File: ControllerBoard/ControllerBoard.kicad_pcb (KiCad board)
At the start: 4 copper layers, 34 x 12 mm, 31 parts, among them J1 X0511WVS-24AS-LPV01, J2 X0511WVS-24AS-LPV01, U1 PLP5860RKPR, U2 LIS2DE12, U3 nRF52810-QCxx, Y1 32.768kHz 12.5pF, Y2 32MHz 8pF <40ppm

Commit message: Minor board updates
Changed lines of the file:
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@@
   (segment (start 135.27 76.75) (end 135.309081 76.789081) (width 0.2) (layer "B.Cu") (net 6))
   (arc (start 135.309081 76.789081) (mid 135.450381 77.000552) (end 135.5 77.25) (width 0.2) (layer "B.Cu") (net 6))
+  (segment (start 134 85.25) (end 134 85.75) (width 0.2) (layer "F.Cu") (net 7))
+  (segment (start 135 82.95) (end 135 84.25) (width 0.2) (layer "F.Cu") (net 7))
   (segment (start 134 86.23) (end 134 85.75) (width 0.2) (layer "F.Cu") (net 7))
   (segment (start 132.75 86.23) (end 134 86.23) (width 0.2) (layer "F.Cu") (net 7))
   (segment (start 135 84.25) (end 134 85.25) (width 0.2) (layer "F.Cu") (net 7))
-  (segment (start 135 82.95) (end 135 84.25) (width 0.2) (layer "F.Cu") (net 7))
-  (segment (start 134 85.25) (end 134 85.75) (width 0.2) (layer "F.Cu") (net 7))
   (segment (start 136.5 86.23) (end 136.5 85.75) (width 0.2) (layer "F.Cu") (net 8))
-  (segment (start 135.5 84.375) (end 136.5 85.375) (width 0.2) (layer "F.Cu") (net 8))
-  (segment (start 135.5 82.95) (end 135.5 84.375) (width 0.2) (layer "F.Cu") (net 8))
+  (segment (start 135.5 82.95) (end 135.5 84.25) (width 0.2) (layer "F.Cu") (net 8))
+  (segment (start 135.5 84.25) (end 136.5 85.25) (width 0.2) (layer "F.Cu") (net 8))
+  (segment (start 136.5 85.25) (end 136.5 85.75) (width 0.2) (layer "F.Cu") (net 8))
   (segment (start 137.75 86.23) (end 136.5 86.23) (width 0.2) (layer "F.Cu") (net 8))
-  (segment (start 136.5 85.375) (end 136.5 85.75) (width 0.2) (layer "F.Cu") (net 8))
   (segment (start 134.5 83.58) (end 133.98 84.1) (width 0.2) (layer "F.Cu") (net 9))
   (segment (start 134.5 82.95) (end 134.5 83.58) (width 0.2) (layer "F.Cu") (net 9))

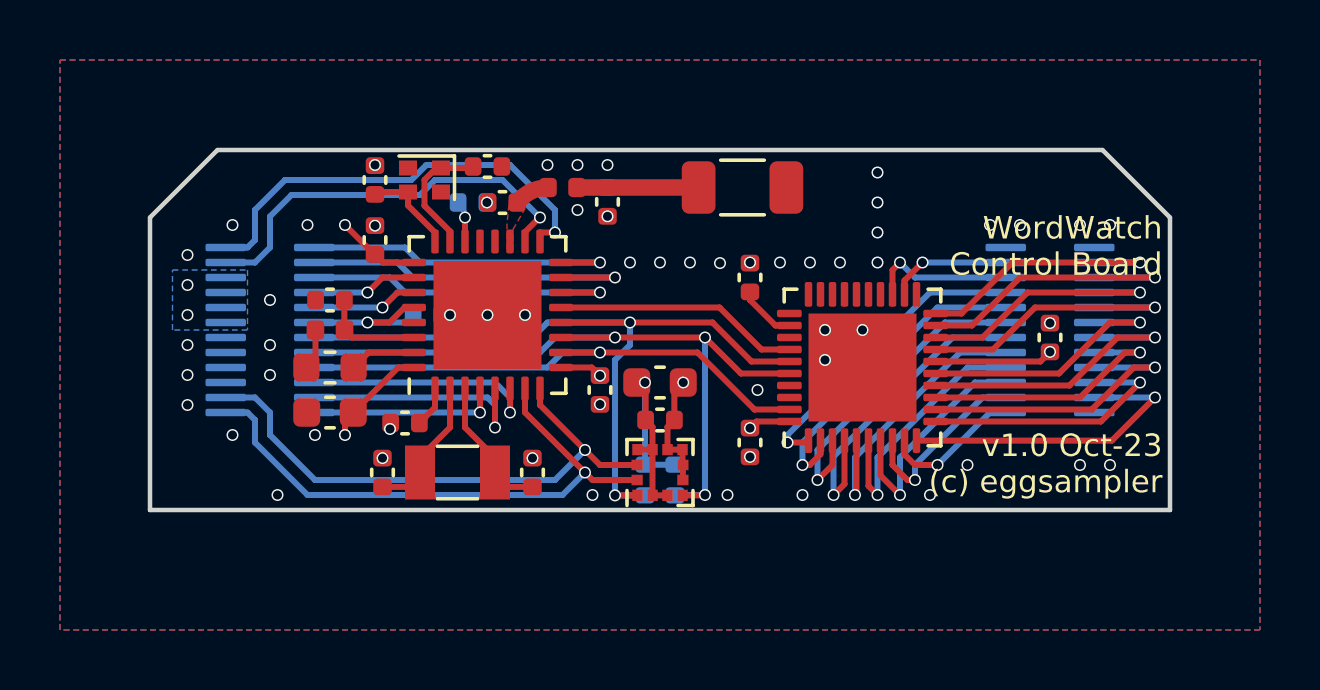
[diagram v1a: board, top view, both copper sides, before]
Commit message: Remove LED driver
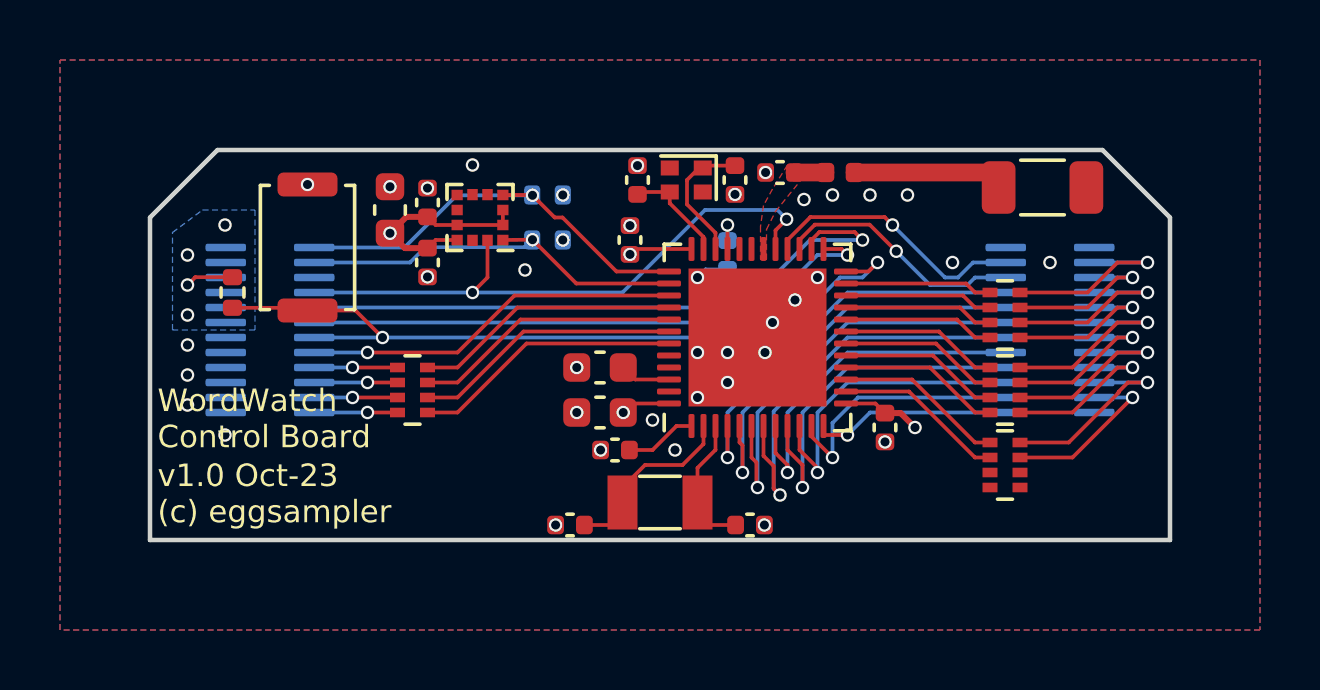
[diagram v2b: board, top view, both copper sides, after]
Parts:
- removed C17: 16p, Capacitor_SMD:C_0402_1005Metric
- removed C18: 10n, Capacitor_SMD:C_0402_1005Metric
- removed C2, C3: 1u, Capacitor_SMD:C_0402_1005Metric
- removed L2: 10uH, Inductor_SMD:L_0603_1608Metric
- removed L3: 3.9nH, Inductor_SMD:L_0402_1005Metric
- removed U1: PLP5860RKPR, Package_DFN_QFN:QFN-40-1EP_5x5mm_P0.4mm_EP3.6x3.6mm
- added R3: 4.7k, Resistor_SMD:R_0402_1005Metric, F.Cu at (127.8, 79.8)
- added RN1: 1k, Resistor_SMD:R_Array_Concave_4x0402, F.Cu at (153.5, 85.5)
- added RN2: 1k, Resistor_SMD:R_Array_Concave_4x0402, F.Cu at (153.5, 83.0)
- added RN3: 1k, Resistor_SMD:R_Array_Concave_4x0402, F.Cu at (153.5, 80.5)
- added RN4: 1k, Resistor_SMD:R_Array_Concave_4x0402, F.Cu at (133.8, 83.0)
- added SW1: RESET, Button_Switch_SMD:SW_Push_SPST_NO_Alps_SKRK, F.Cu at (130.2, 78.2)
- C1: value 1u -> 100n
- C11: value 100n -> 100p; moved to B.Cu
- C12: value 25p -> 12p
- C15: value 0.8p -> 12p
- C16: value 16p -> 12p
- C6: footprint Capacitor_SMD:C_0402_1005Metric -> Capacitor_SMD:C_0603_1608Metric
- C7: value 100p -> 12p; moved to F.Cu
- C8: value 25p -> 4.7u; footprint Capacitor_SMD:C_0402_1005Metric -> Capacitor_SMD:C_0603_1608Metric
- C9: value 4.7u -> 100n; footprint Capacitor_SMD:C_0603_1608Metric -> Capacitor_SMD:C_0402_1005Metric
- L1: value 15nH -> 3.9nH
- U3: value nRF52810-QCxx -> nRF52810-QFxx; footprint Package_DFN_QFN:QFN-32-1EP_5x5mm_P0.5mm_EP3.6x3.6mm -> Package_DFN_QFN:QFN-48-1EP_6x6mm_P0.4mm_EP4.6x4.6mm
- Y1: value 32.768kHz 12.5pF -> 32.768kHz
- Y2: value 32MHz 8pF <40ppm -> 32MHz
- moved C1 20.9 mm to (134.2, 78.8), turned to -90 degrees
- moved C10 18.1 mm to (149.5, 84.2), turned to -90 degrees
- moved L1 17.8 mm to (148.0, 75.8)
- moved C9 11.5 mm to (141.0, 78.0), turned to 90 degrees
- moved C7 11.2 mm to (139.0, 87.5), turned to 180 degrees
- moved C5 10.7 mm to (133.0, 77.0), turned to 90 degrees
- moved C4 10.6 mm to (134.2, 76.8), turned to 90 degrees
- moved R1 10.4 mm to (138.2, 76.5), turned to 0 degrees
- moved U2 10.4 mm to (136.0, 77.2), turned to 180 degrees
- moved AE1 10.0 mm to (154.8, 76.2)
- moved C6 9.28 mm to (140.0, 82.2)
- moved U3 9.03 mm to (145.2, 81.2)
- moved Y2 8.72 mm to (142.9, 76.0)
- moved R2 8.63 mm to (138.2, 78.0), turned to 180 degrees
- moved C15 7.79 mm to (144.5, 76.0), turned to 90 degrees
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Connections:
- C11 pad 1: VCC -> /Microcontroller/DEC3
- C12 pad 1: GND -> /Microcontroller/XL2
- C12 pad 2: /Microcontroller/XL2 -> GND
- C14 pad 1: /Microcontroller/ANT2 -> /Microcontroller/ANT1
- C15 pad 1: /Microcontroller/ANT1 -> GND
- C15 pad 2: GND -> /Microcontroller/XC1
- C16 pad 2: /Microcontroller/XC1 -> /Microcontroller/XC2
- C7 pad 1: /Microcontroller/DEC3 -> /Microcontroller/XL1
- C8 pad 1: GND -> VCC
- C8 pad 2: /Microcontroller/XL1 -> GND
- J2 pad 1: /Connectors/RESET -> /Accelerometer/SDA
- J2 pad 11: /Connectors/VSENSE -> /Connectors/SWDCLK
- J2 pad 13: /Accelerometer/SCL -> /Microcontroller/RESET
- J2 pad 15: /Accelerometer/SDA -> /Connectors/BUTTON
- J2 pad 17: /Connectors/LED_EN -> /Connectors/LED0
- J2 pad 19: /Connectors/LED2 -> /Connectors/LED1
- J2 pad 2: /Connectors/SWDCLK -> VCC
- J2 pad 21: /Connectors/LED3 -> /Connectors/LED2
- J2 pad 22: /Accelerometer/INT2 -> GND
- J2 pad 23: /Connectors/BUTTON -> /Connectors/LED3
- J2 pad 24: /Accelerometer/INT1 -> GND
- J2 pad 3: /Connectors/TX -> /Accelerometer/SCL
- J2 pad 4: /Connectors/SWDIO -> VCC
- J2 pad 5: /Connectors/RX -> GND
- J2 pad 7: /Connectors/LED0 -> /Accelerometer/INT1
- J2 pad 9: /Connectors/LED1 -> /Connectors/SWDIO
- L1 pad 1: /Microcontroller/DEC4 -> /Microcontroller/ANT2
- L1 pad 2: Net-(L1-Pad2) -> /Microcontroller/ANT1
- U2 pad 11: /Accelerometer/INT2 -> unconnected-(U2-INT2-Pad11)
- U3 pad 10: /Connectors/LED_EN -> /Connectors/COL6
- U3 pad 11: /Accelerometer/SDA -> /Connectors/COL7
- U3 pad 12: /Accelerometer/SCL -> /Connectors/COL8
- U3 pad 13: /LED Driver/VSYNC -> VCC
- U3 pad 14: /Connectors/RX -> /Microcontroller/ROW9_R
- U3 pad 15: /Connectors/TX -> /Microcontroller/ROW8_R
- U3 pad 16: /Connectors/RESET -> /Microcontroller/ROW7_R
- U3 pad 17: /Connectors/SWDCLK -> /Microcontroller/ROW6_R
- U3 pad 18: /Connectors/SWDIO -> /Microcontroller/ROW5_R
- U3 pad 19: /Microcontroller/ANT1 -> /Microcontroller/ROW4_R
- U3 pad 20: GND -> /Microcontroller/ROW3_R
- U3 pad 21: unconnected-(U3-DEC2-Pad21) -> /Microcontroller/ROW2_R
- U3 pad 22: /Microcontroller/DEC3 -> /Microcontroller/ROW1_R
- U3 pad 23: /Microcontroller/XC1 -> /Microcontroller/ROW0_R
- U3 pad 24: /Microcontroller/XC2 -> /Microcontroller/RESET
- U3 pad 25: VCC -> /Connectors/SWDCLK
- U3 pad 26: /Connectors/LED0 -> /Connectors/SWDIO
- U3 pad 27: /Connectors/LED1 -> /Connectors/COL10
- U3 pad 28: /Connectors/VSENSE -> /Connectors/COL9
- U3 pad 29: GND -> /Accelerometer/INT1
- U3 pad 30: /Microcontroller/DEC4 -> /Microcontroller/ANT1
- U3 pad 31: /Microcontroller/DCC -> GND
- U3 pad 32: VCC -> unconnected-(U3-DEC2-Pad32)
- U3 pad 33: GND -> /Microcontroller/DEC3
- U3 pad 4: /Connectors/BUTTON -> /Connectors/COL0
- U3 pad 5: /Connectors/LED3 -> /Connectors/COL1
- U3 pad 6: /Connectors/LED2 -> /Connectors/COL2
- U3 pad 7: /Accelerometer/INT1 -> /Connectors/COL3
- U3 pad 8: /Accelerometer/INT2 -> /Connectors/COL4
- U3 pad 9: VCC -> /Connectors/COL5
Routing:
- net /Microcontroller/RESET: track 0.00 -> 26.4 mm, vias 0 -> 2
- net /Accelerometer/INT2: track 18.6 -> 0.00 mm, vias 1 -> 0
- net /Connectors/LED_EN: track 18.1 -> 0.00 mm, vias 1 -> 0
- net /Accelerometer/SCL: track 26.6 -> 13.7 mm, vias 2 -> 1
- net /Connectors/TX: track 12.0 -> 0.00 mm, vias 1 -> 0
- net /Connectors/RX: track 11.0 -> 0.00 mm, vias 1 -> 0
- net /Connectors/RESET: track 11.0 -> 0.00 mm, vias 1 -> 0
- net /Accelerometer/SDA: track 25.3 -> 14.6 mm, vias 3 -> 1
- net /Microcontroller/LED3_R: track 0.00 -> 9.00 mm
- net /Microcontroller/LED2_R: track 0.00 -> 8.96 mm
- net /Microcontroller/LED1_R: track 0.00 -> 8.92 mm
- net /Microcontroller/LED0_R: track 0.00 -> 8.88 mm
- net /LED Driver/VSYNC: track 8.19 -> 0.00 mm
- net /Connectors/SWDIO: track 13.8 -> 21.4 mm
- net VCC: track 21.8 -> 15.2 mm, vias 8 -> 10
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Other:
- board size 34 x 12 mm -> 34 x 13 mm

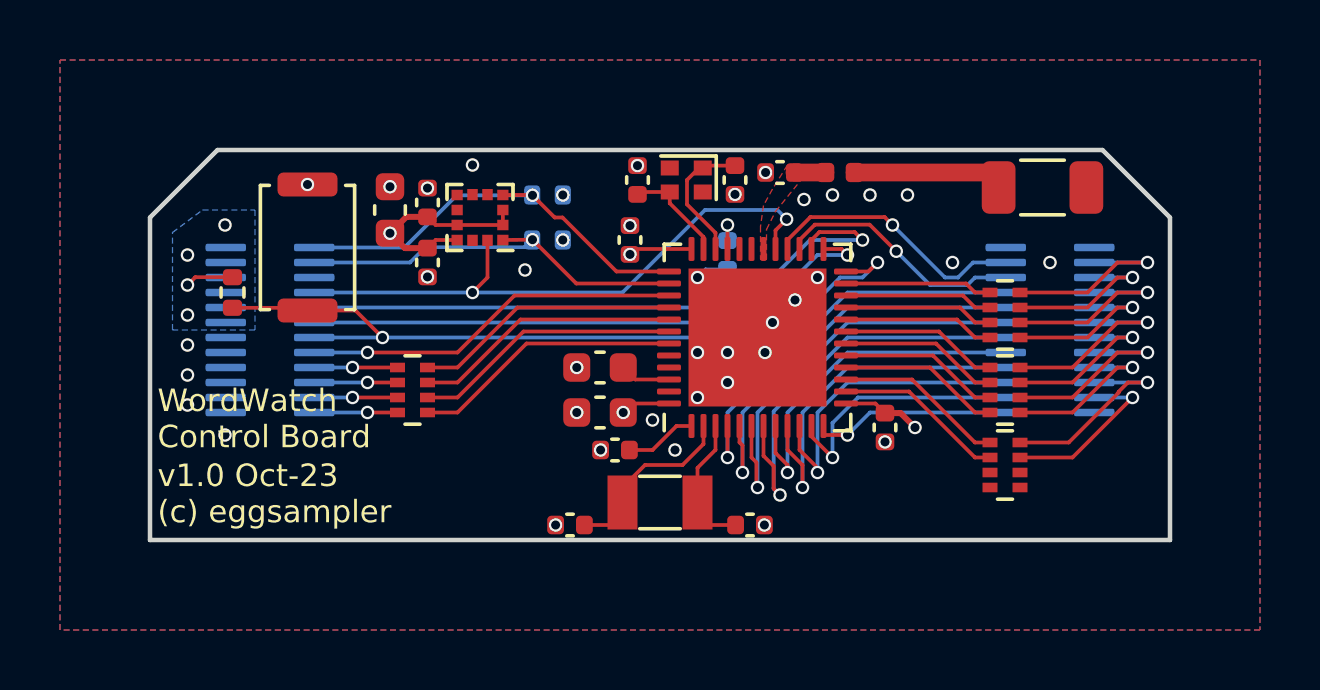
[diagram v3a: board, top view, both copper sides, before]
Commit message: Remove all via in pad on controller board where possible
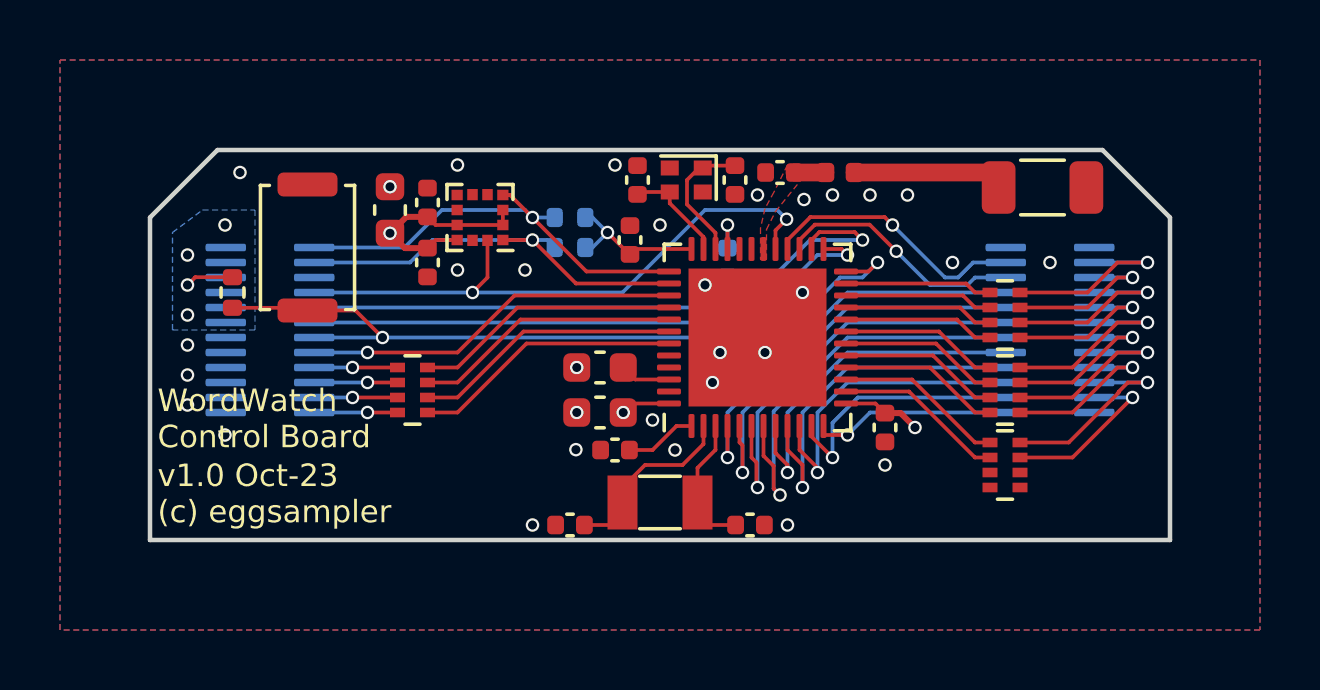
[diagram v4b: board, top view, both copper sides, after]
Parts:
- moved R1 1.06 mm to (139.0, 77.2)
- moved R2 0.79 mm to (139.0, 78.2)
- moved C11 0.25 mm to (144.2, 78.8)
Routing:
- net VCC: track 15.2 -> 18.0 mm, vias 10 -> 8
- net GND: track 1.11 -> 0.00 mm, vias 37 -> 31
- net /Accelerometer/SCL: track 13.7 -> 14.6 mm
- net /Accelerometer/SDA: track 14.6 -> 15.2 mm

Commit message: Change led matrix routing for sinking current through mcu, sourcing from battery
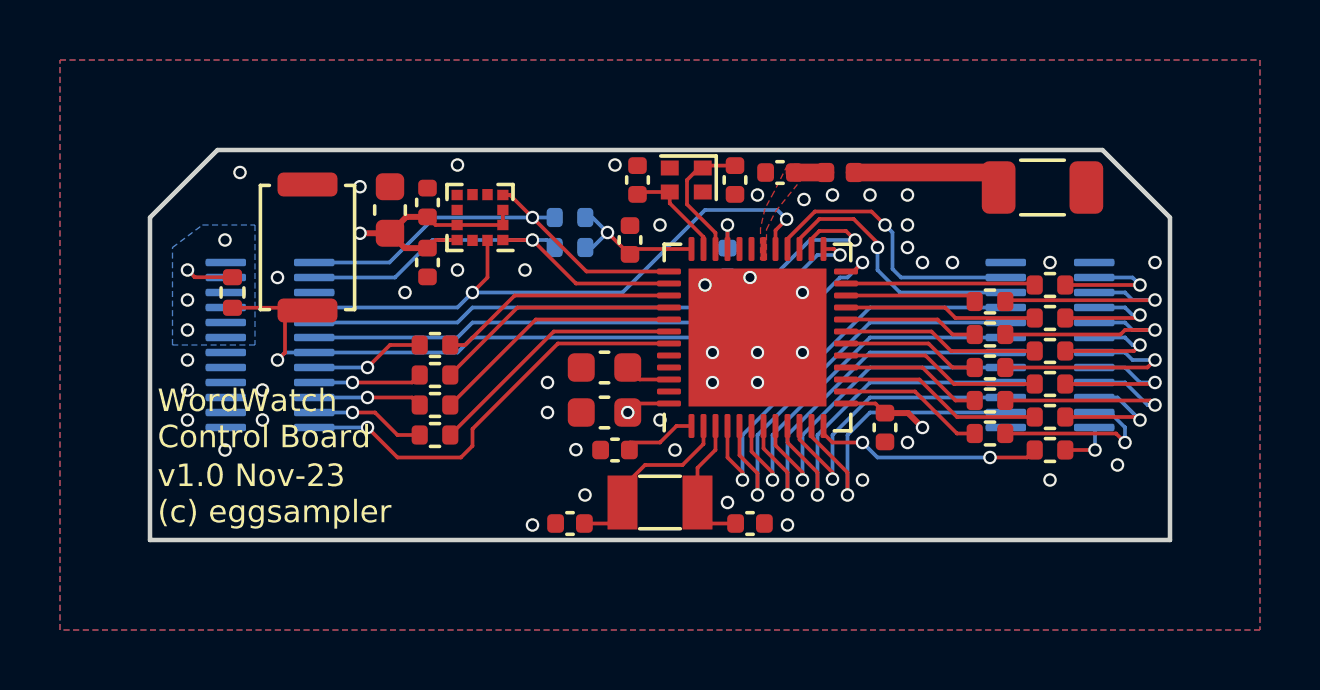
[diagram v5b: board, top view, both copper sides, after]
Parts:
- removed RN1, RN2, RN3, RN4: 1k, Resistor_SMD:R_Array_Concave_4x0402
- added R10: 1k, Resistor_SMD:R_0402_1005Metric, F.Cu at (155.0, 82.8)
- added R11: 1k, Resistor_SMD:R_0402_1005Metric, F.Cu at (153.0, 83.3)
- added R12: 1k, Resistor_SMD:R_0402_1005Metric, F.Cu at (155.0, 83.9)
- added R13: 1k, Resistor_SMD:R_0402_1005Metric, F.Cu at (153.0, 84.5)
- added R14: 1k, Resistor_SMD:R_0402_1005Metric, F.Cu at (155.0, 85.0)
- added R15: 1k, Resistor_SMD:R_0402_1005Metric, F.Cu at (134.5, 81.5)
- added R16: 1k, Resistor_SMD:R_0402_1005Metric, F.Cu at (134.5, 82.5)
- added R17: 1k, Resistor_SMD:R_0402_1005Metric, F.Cu at (134.5, 83.5)
- added R18: 1k, Resistor_SMD:R_0402_1005Metric, F.Cu at (134.5, 84.5)
- added R4: 1k, Resistor_SMD:R_0402_1005Metric, F.Cu at (155.0, 79.5)
- added R5: 1k, Resistor_SMD:R_0402_1005Metric, F.Cu at (153.0, 80.0)
- added R6: 1k, Resistor_SMD:R_0402_1005Metric, F.Cu at (155.0, 80.6)
- added R7: 1k, Resistor_SMD:R_0402_1005Metric, F.Cu at (153.0, 81.2)
- added R8: 1k, Resistor_SMD:R_0402_1005Metric, F.Cu at (155.0, 81.7)
- added R9: 1k, Resistor_SMD:R_0402_1005Metric, F.Cu at (153.0, 82.2)
- moved J1 0.50 mm to (155.0, 81.5)
- moved J2 0.50 mm to (129.0, 81.5)
- moved C6 0.15 mm to (140.2, 82.2)
- moved C8 0.15 mm to (140.2, 83.8)
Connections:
- J1 pad 10: /Connectors/COL1 -> /Connectors/ROW3
- J1 pad 11: /Connectors/ROW4 -> /Connectors/COL4
- J1 pad 12: /Connectors/COL2 -> /Connectors/ROW4
- J1 pad 13: /Connectors/ROW5 -> /Connectors/COL5
- J1 pad 14: /Connectors/COL3 -> /Connectors/ROW5
- J1 pad 15: /Connectors/ROW6 -> /Connectors/COL6
- J1 pad 16: /Connectors/COL4 -> /Connectors/ROW6
- J1 pad 17: /Connectors/ROW7 -> /Connectors/COL7
- J1 pad 18: /Connectors/COL5 -> /Connectors/ROW7
- J1 pad 19: /Connectors/ROW8 -> /Connectors/COL8
- J1 pad 20: /Connectors/COL6 -> /Connectors/ROW8
- J1 pad 21: /Connectors/ROW9 -> /Connectors/COL9
- J1 pad 22: /Connectors/COL7 -> /Connectors/ROW9
- J1 pad 23: GND -> /Connectors/COL10
- J1 pad 24: /Connectors/COL8 -> GND
- J1 pad 3: /Connectors/ROW0 -> /Connectors/COL0
- J1 pad 4: /Connectors/COL9 -> /Connectors/ROW0
- J1 pad 5: /Connectors/ROW1 -> /Connectors/COL1
- J1 pad 6: /Connectors/COL10 -> /Connectors/ROW1
- J1 pad 7: /Connectors/ROW2 -> /Connectors/COL2
- J1 pad 8: /Connectors/COL0 -> /Connectors/ROW2
- J1 pad 9: /Connectors/ROW3 -> /Connectors/COL3
- J2 pad 15: /Connectors/BUTTON -> /Connectors/LED0
- J2 pad 17: /Connectors/LED0 -> /Connectors/LED1
- J2 pad 19: /Connectors/LED1 -> /Connectors/LED2
- J2 pad 21: /Connectors/LED2 -> /Connectors/LED3
- J2 pad 23: /Connectors/LED3 -> /Connectors/BUTTON
- U3 pad 10: /Connectors/COL6 -> /Connectors/ROW8
- U3 pad 11: /Connectors/COL7 -> /Connectors/ROW9
- U3 pad 12: /Connectors/COL8 -> /Microcontroller/COL10_R
- U3 pad 14: /Microcontroller/ROW9_R -> /Microcontroller/COL9_R
- U3 pad 15: /Microcontroller/ROW8_R -> /Microcontroller/COL8_R
- U3 pad 16: /Microcontroller/ROW7_R -> /Microcontroller/COL7_R
- U3 pad 17: /Microcontroller/ROW6_R -> /Microcontroller/COL6_R
- U3 pad 18: /Microcontroller/ROW5_R -> /Microcontroller/COL5_R
- U3 pad 19: /Microcontroller/ROW4_R -> /Microcontroller/COL4_R
- U3 pad 20: /Microcontroller/ROW3_R -> /Microcontroller/COL3_R
- U3 pad 21: /Microcontroller/ROW2_R -> /Microcontroller/COL2_R
- U3 pad 22: /Microcontroller/ROW1_R -> /Microcontroller/COL1_R
- U3 pad 23: /Microcontroller/ROW0_R -> /Microcontroller/COL0_R
- U3 pad 27: /Connectors/COL10 -> /Connectors/ROW1
- U3 pad 28: /Connectors/COL9 -> /Connectors/ROW0
- U3 pad 39: /Connectors/BUTTON -> /Microcontroller/LED0_R
- U3 pad 4: /Connectors/COL0 -> /Connectors/ROW2
- U3 pad 40: /Microcontroller/LED0_R -> /Microcontroller/LED1_R
- U3 pad 41: /Microcontroller/LED1_R -> /Microcontroller/LED2_R
- U3 pad 42: /Microcontroller/LED2_R -> /Microcontroller/LED3_R
- U3 pad 43: /Microcontroller/LED3_R -> /Connectors/BUTTON
- U3 pad 5: /Connectors/COL1 -> /Connectors/ROW3
- U3 pad 6: /Connectors/COL2 -> /Connectors/ROW4
- U3 pad 7: /Connectors/COL3 -> /Connectors/ROW5
- U3 pad 8: /Connectors/COL4 -> /Connectors/ROW6
- U3 pad 9: /Connectors/COL5 -> /Connectors/ROW7
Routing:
- net /Connectors/COL2: track 14.2 -> 4.16 mm
- net /Connectors/COL0: track 13.5 -> 4.12 mm
- net /Connectors/ROW3: track 5.44 -> 14.4 mm
- net /Microcontroller/COL10_R: track 0.00 -> 7.72 mm, vias 0 -> 2
- net /Connectors/COL4: track 11.8 -> 4.20 mm
- net /Connectors/ROW2: track 6.44 -> 14.0 mm
- net /Connectors/ROW5: track 5.65 -> 13.0 mm
- net /Connectors/COL3: track 14.2 -> 7.18 mm
- net /Microcontroller/COL8_R: track 0.00 -> 6.81 mm
- net /Microcontroller/COL6_R: track 0.00 -> 6.68 mm
- net /Connectors/COL1: track 13.8 -> 7.14 mm
- net /Connectors/COL10: track 8.32 -> 1.75 mm
- net /Microcontroller/COL4_R: track 0.00 -> 6.56 mm
- net /Microcontroller/COL2_R: track 0.00 -> 6.43 mm
- net /Microcontroller/COL0_R: track 0.00 -> 6.31 mm
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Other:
- board text added: "v1.0 Nov-23 (c) eggsampler"
- board text removed: "v1.0 Oct-23 (c) eggsampler"
